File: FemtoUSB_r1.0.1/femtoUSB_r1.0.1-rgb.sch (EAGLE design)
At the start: 33 parts, among them IC1 ATSAMD21E18A-MUT

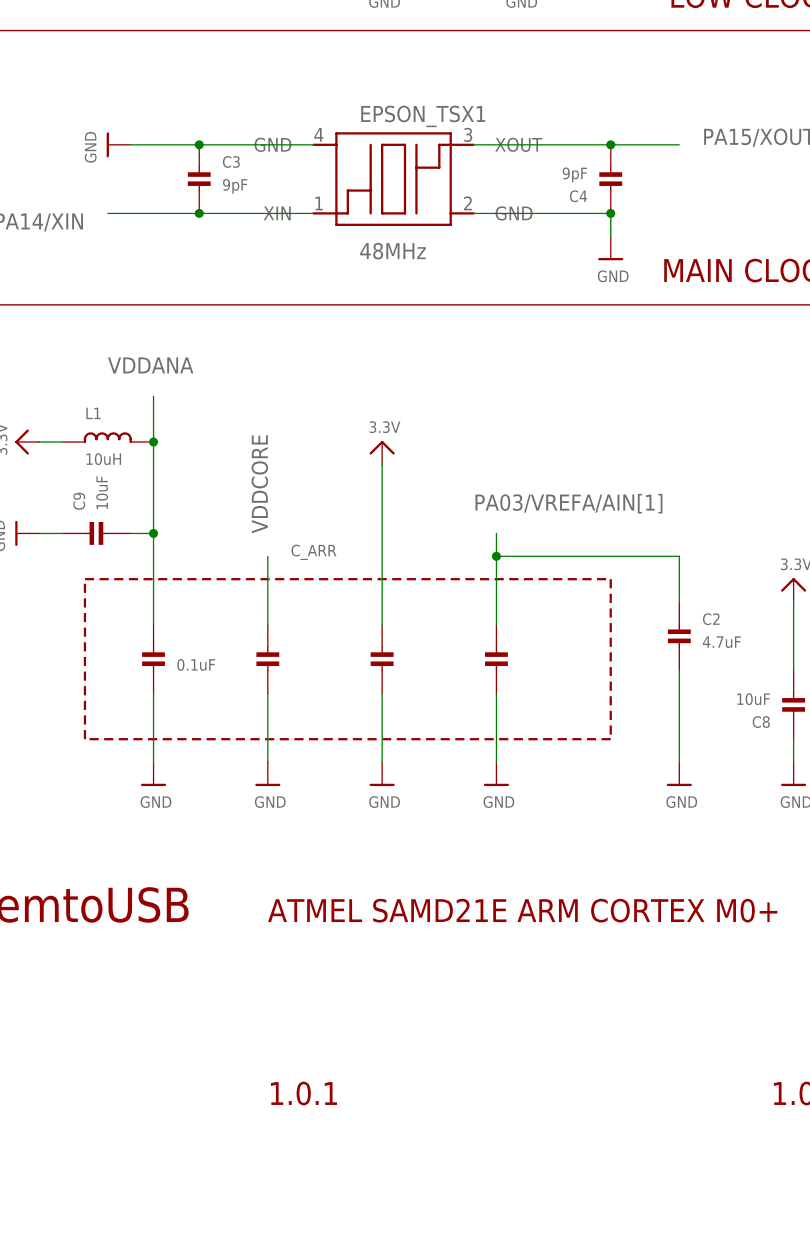
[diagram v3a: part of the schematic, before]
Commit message: Caps for 48MHz updated from 9pF to 10pF. Updated to correct manufacturor ID for too. Minor fix to skewed polygon - was supposed to be rectangular.
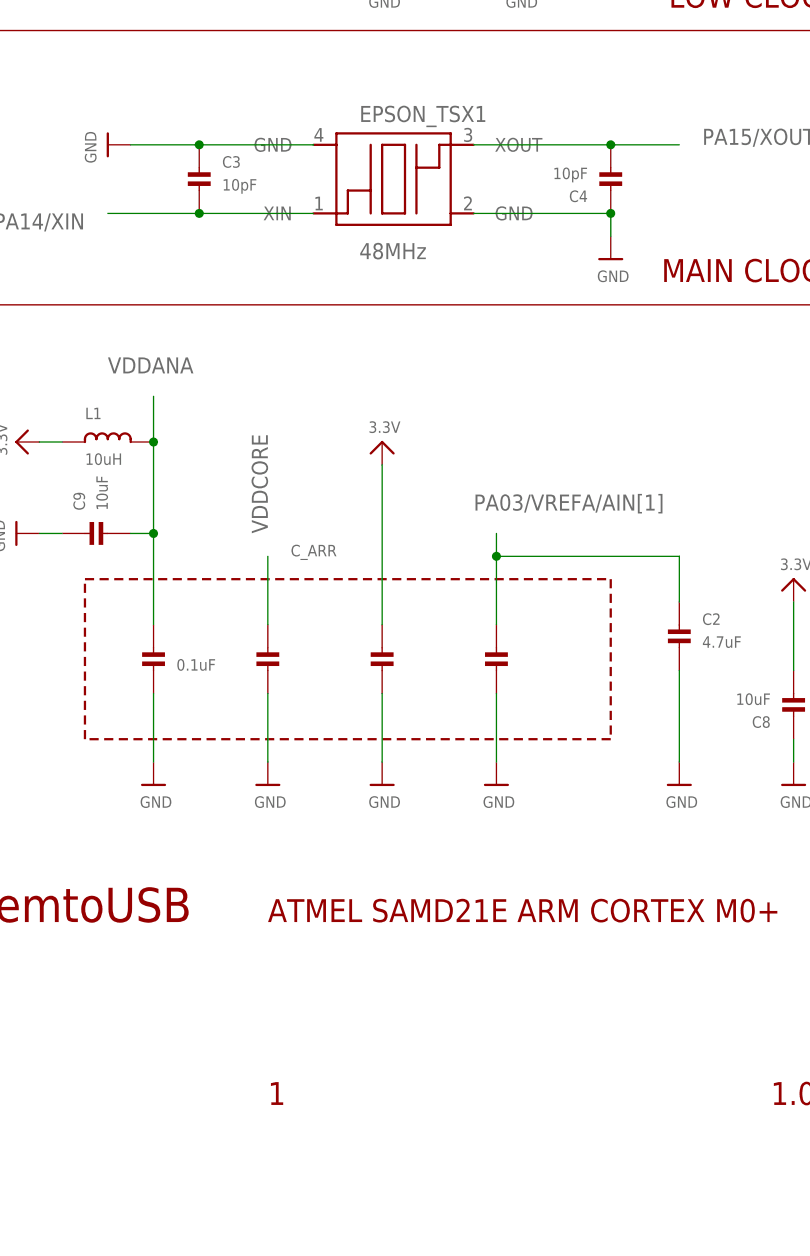
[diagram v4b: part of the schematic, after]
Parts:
- C3, C4: value 9pF -> 10pF; MFR_ID GRM0335C1E100JA01D -> VJ0402A100FXACW1BC
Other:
- note added: "1"
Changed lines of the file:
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@@
 <attribute name="MFR_ID" value="C1005X5R1A475K050BC"/>
 </part>
-<part name="C3" library="microbuilder" deviceset="CAP_CERAMIC" device="_0402MP" value="9pF">
-<attribute name="MFR_ID" value="GRM0335C1E100JA01D"/>
+<part name="C3" library="microbuilder" deviceset="CAP_CERAMIC" device="_0402MP" value="10pF">
+<attribute name="MFR_ID" value="VJ0402A100FXACW1BC"/>
 </part>
-<part name="C4" library="microbuilder" deviceset="CAP_CERAMIC" device="_0402MP" value="9pF">
-<attribute name="MFR_ID" value="GRM0335C1E100JA01D"/>
+<part name="C4" library="microbuilder" deviceset="CAP_CERAMIC" device="_0402MP" value="10pF">
+<attribute name="MFR_ID" value="VJ0402A100FXACW1BC"/>
 </part>
 <part name="R2" library="microbuilder" deviceset="RESISTOR" device="_0402MP" value="10K">
@@
 <text x="149.86" y="27.94" size="3.81" layer="94" font="vector">FemtoUSB</text>
 <text x="238.76" y="7.62" size="2.54" layer="94" font="vector">1.0.1</text>
-<text x="182.88" y="7.62" size="2.54" layer="94" font="vector">1.0.1</text>
+<text x="182.88" y="7.62" size="2.54" layer="94" font="vector">1</text>
 <text x="182.88" y="27.94" size="2.54" layer="94" font="vector">ATMEL SAMD21E ARM CORTEX M0+</text>
 <wire x1="0" y1="60.96" x2="73.66" y2="60.96" width="0.1524" layer="94"/>
